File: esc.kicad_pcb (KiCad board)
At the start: 4 copper layers, 68.3 x 63.8 mm, 73 parts, among them J1 Conn_01x02, J2 Screw_Terminal_01x01, J3 Screw_Terminal_01x01, J4 Screw_Terminal_01x01, J5 3220-10-0100-00, Q1 SIR182DP-T1-RE3, Q2 SIR182DP-T1-RE3, Q3 SIR182DP-T1-RE3, Q4 SIR182DP-T1-RE3, Q5 SIR182DP-T1-RE3, Q6 SIR182DP-T1-RE3, SW1 RotaryEncoder, U1 TPS7A20xxxDQN, U2 STM32G484CETx, U3 TPS562201DDCR, U4 TVS0500DRV, U5 IR2103STRPBF, U6 IR2103STRPBF, U7 IR2103STRPBF, Y1 32.768KHz

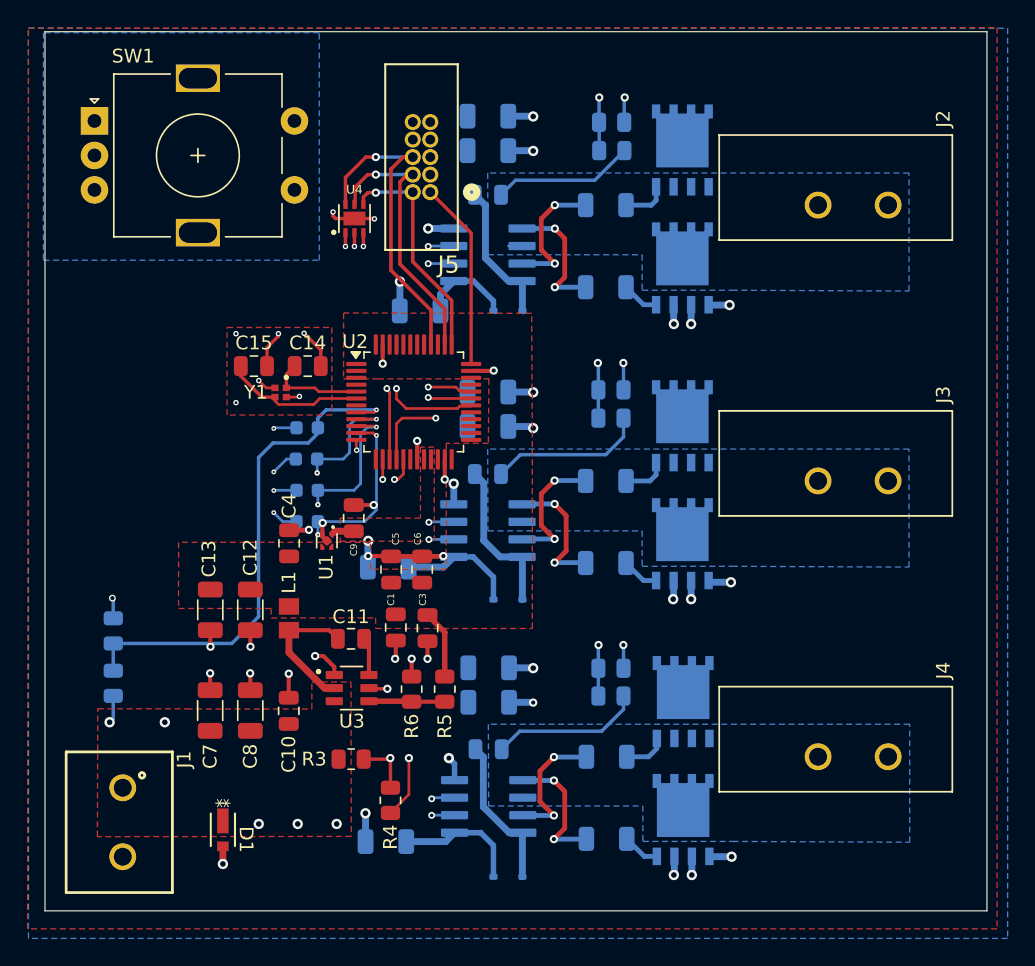
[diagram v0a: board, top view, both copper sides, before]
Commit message: improving MOSFET decap placements
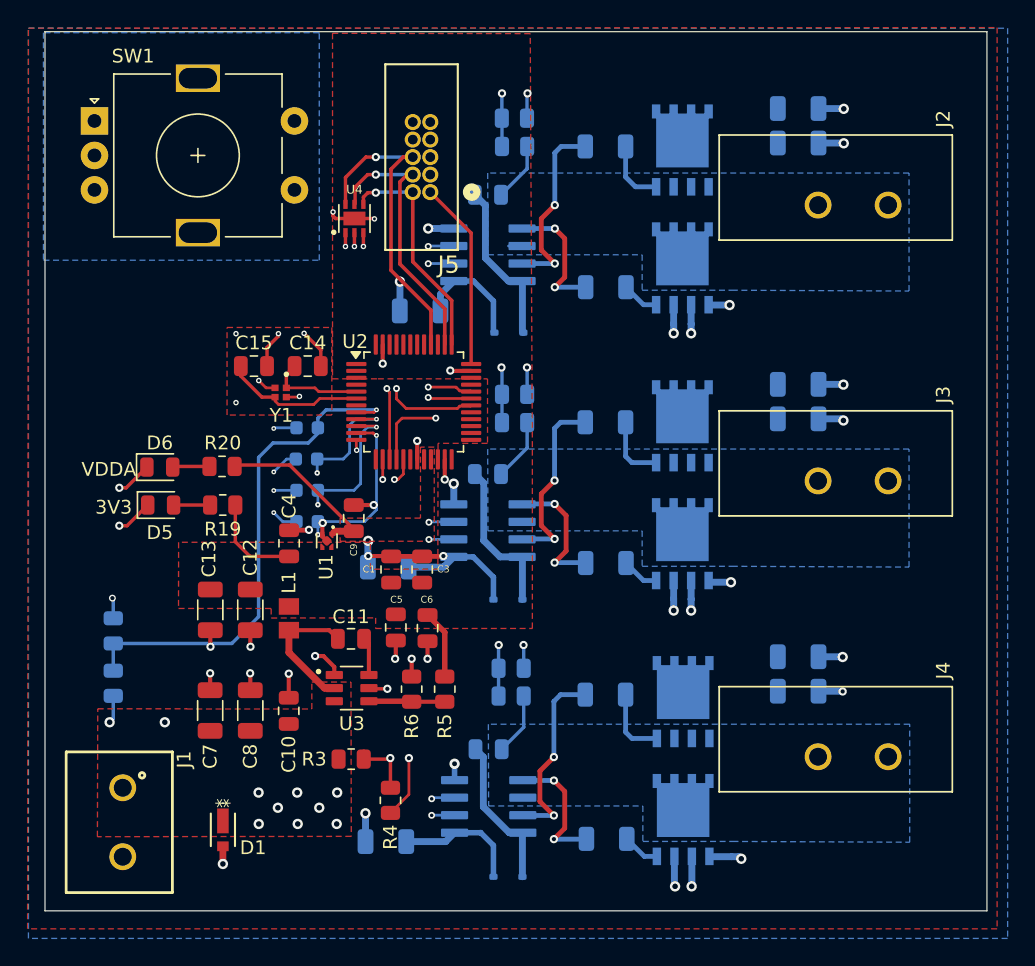
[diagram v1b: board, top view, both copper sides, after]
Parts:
- added D5: LED, LED_SMD:LED_0805_2012Metric, F.Cu at (118.5, 96.8)
- added D6: LED, LED_SMD:LED_0805_2012Metric, F.Cu at (118.4, 94.0)
- added R19: 300, Resistor_SMD:R_0805_2012Metric, F.Cu at (123.0, 96.8)
- added R20: 300, Resistor_SMD:R_0805_2012Metric, F.Cu at (123.0, 94.0)
- moved C18 22.5 mm to (164.7, 68.0)
- moved C19 22.5 mm to (164.7, 70.5)
- moved C23 22.5 mm to (164.7, 88.0)
- moved C24 22.5 mm to (164.7, 90.5)
- moved C28 22.5 mm to (164.7, 107.8)
- moved C29 22.5 mm to (164.7, 110.2)
- moved R17 7.24 mm to (143.9, 110.6)
- moved R18 7.24 mm to (143.9, 108.6)
- moved R9 7.06 mm to (144.2, 70.8)
- moved R10 7.06 mm to (144.2, 68.7)
- moved R13 7.00 mm to (144.2, 90.8)
- moved R14 7.00 mm to (144.2, 88.7)
- moved R15 4.51 mm to (150.8, 110.5)
- moved R11 4.26 mm to (150.8, 90.8)
- moved R7 4.26 mm to (150.8, 70.8)
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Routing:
- net /STM32/W_VSENSE: track 74.1 -> 59.6 mm
- net VDDA: track 1.53 -> 12.3 mm
- net GND: track 97.9 -> 107.9 mm, vias 60 -> 64
- net +3V3: track 18.7 -> 25.7 mm
- net /STM32/U_VSENSE: track 57.9 -> 51.0 mm
- net /V PHASE/V_PHASE: track 11.4 -> 4.51 mm
- net /STM32/V_VSENSE: track 64.2 -> 57.7 mm
- net /W PHASE/W_PHASE: track 11.0 -> 4.52 mm
- net /U PHASE/U_PHASE: track 11.3 -> 5.27 mm
- net Net-(U7-HO): track 9.69 -> 14.0 mm
- net Net-(U5-HO): track 9.66 -> 13.6 mm
- net Net-(U6-HO): track 9.64 -> 13.6 mm
- net /PWR/VDDA_IND: track 0.00 -> 2.68 mm
- net /PWR/3V3_IND: track 0.00 -> 2.65 mm
- net Net-(Q5-Pad4): track 3.16 -> 5.17 mm
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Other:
- board text added: "3V3"
- board text added: "VDDA"

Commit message: fab outputs
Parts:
- removed C6: .1uF, Capacitor_SMD:C_0805_2012Metric
- moved C13 13.3 mm to (135.4, 104.8)
- moved C5 11.4 mm to (141.2, 95.8), turned to 0 degrees
- moved R4 8.35 mm to (142.2, 113.8)
- moved R3 7.74 mm to (139.9, 113.8), turned to -90 degrees
- moved C12 7.70 mm to (132.7, 104.8)
- moved C1 6.11 mm to (141.2, 100.5), turned to 0 degrees
- moved C3 5.02 mm to (141.2, 98.1), turned to 0 degrees
- moved C4 4.25 mm to (132.0, 98.8)
- moved R5 3.95 mm to (137.6, 113.8)
- moved R6 3.93 mm to (135.2, 113.8)
- moved C9 3.67 mm to (136.0, 98.8), turned to -90 degrees
- moved U1 3.53 mm to (134.0, 98.6)
- moved C11 2.30 mm to (131.2, 108.5)
- moved U3 2.04 mm to (131.2, 111.8)
- moved L1 1.07 mm to (126.8, 104.8)
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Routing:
- net GND: track 107.9 -> 81.4 mm, vias 64 -> 49
- net VCC: track 28.4 -> 39.6 mm, vias 10 -> 9
- net VDDA: track 12.3 -> 22.8 mm
- net /PWR/BST: track 9.86 -> 0.00 mm
- net +3V3: track 25.7 -> 35.2 mm
- net /PWR/VFB: track 5.52 -> 6.48 mm
- added copper zone on F.Cu, net /PWR/BST
- removed copper zone on F.Cu, net VDDA
